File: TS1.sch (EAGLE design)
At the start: 20 parts, among them IC1 AT42QT1010, J1 PWR, Q1 2N7002

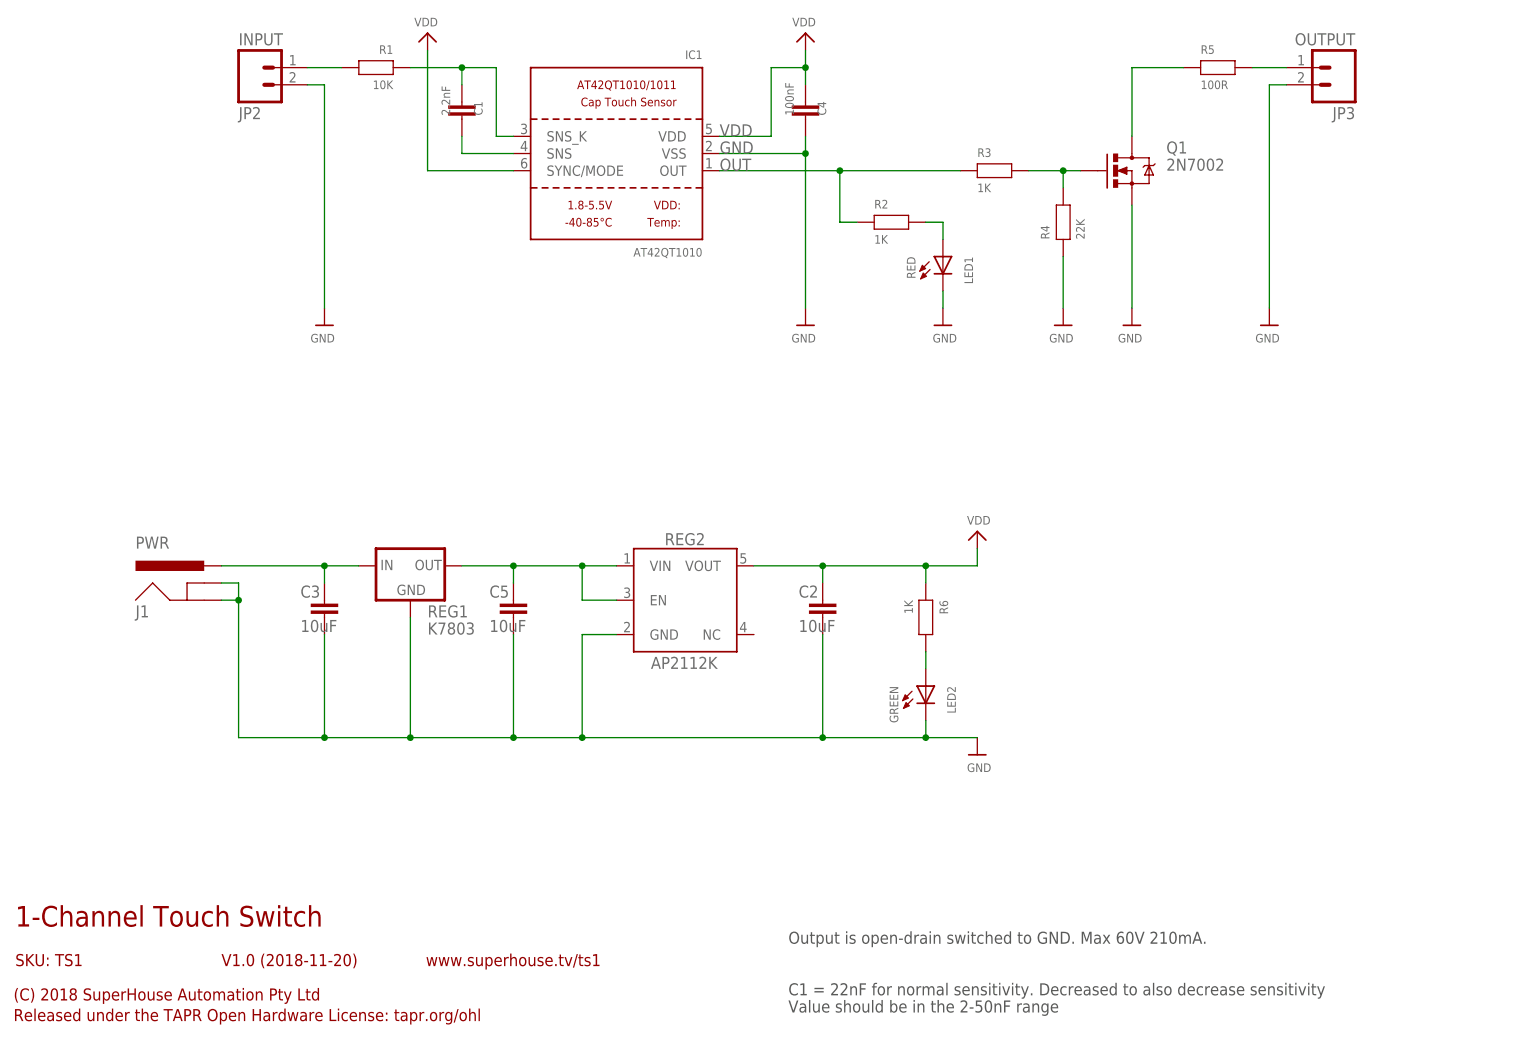
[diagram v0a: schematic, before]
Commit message: Pulled back GND plane around input to sensor IC to reduce capacitive loading
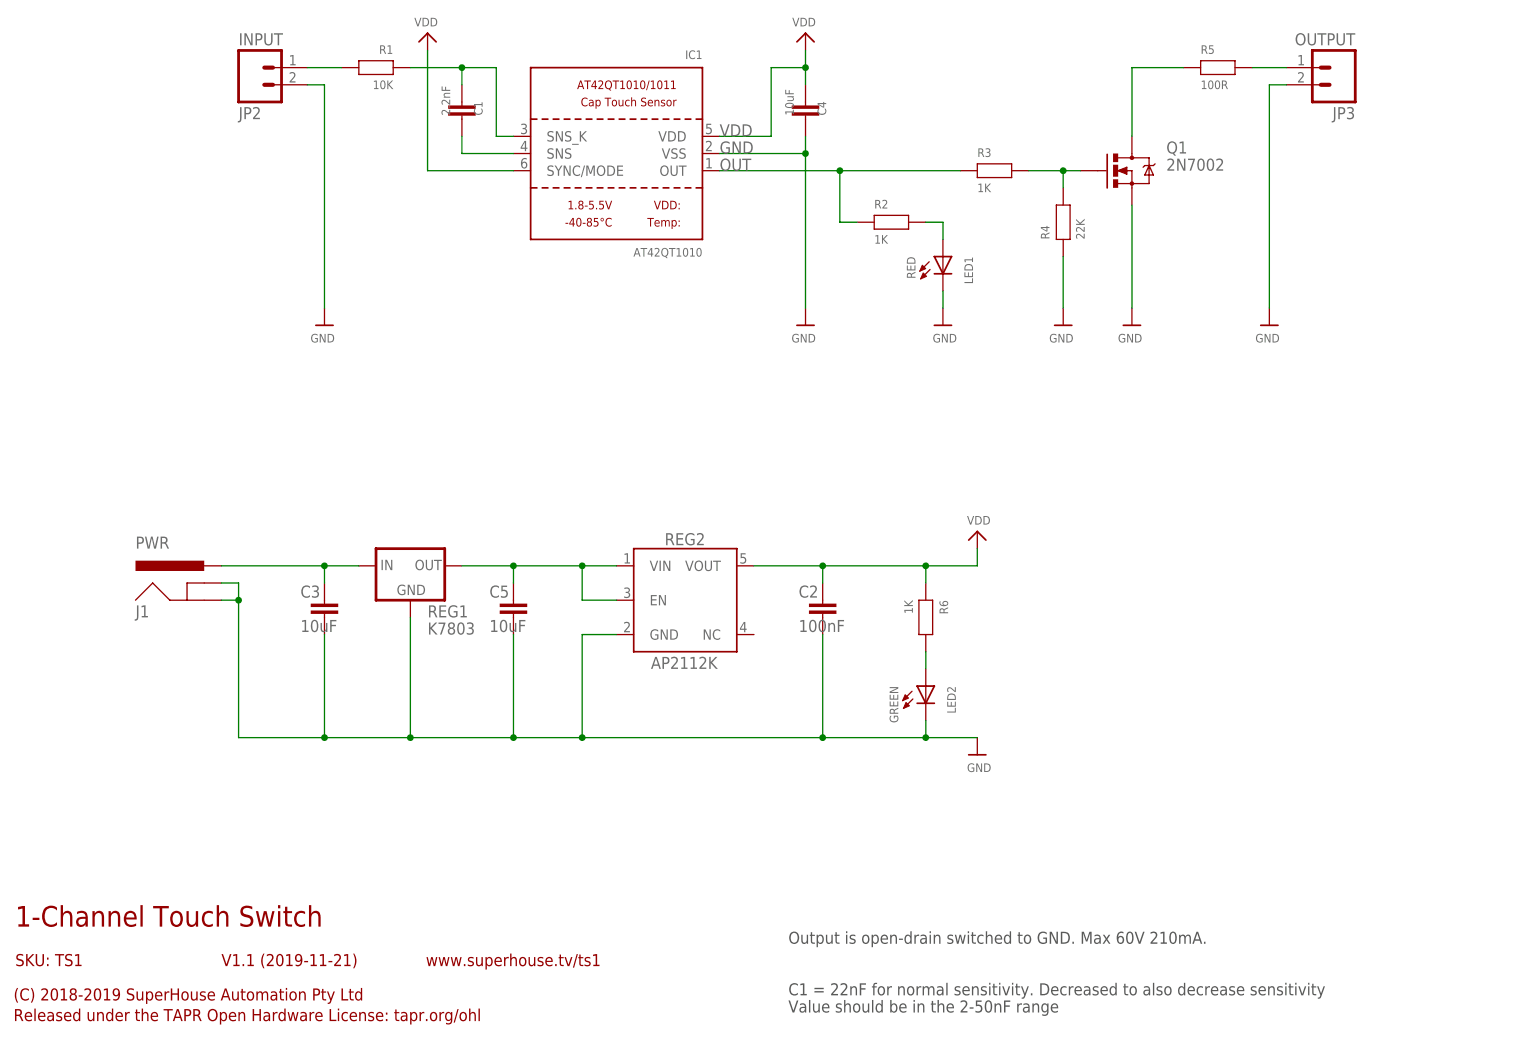
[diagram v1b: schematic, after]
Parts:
- C2: value 10uF -> 100nF
- C4: value 100nF -> 10uF
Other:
- note added: "(C) 2018-2019 SuperHouse Automation Pty Ltd"
- note added: "V1.1 (2019-11-21)"
- note removed: "(C) 2018 SuperHouse Automation Pty Ltd"
- note removed: "V1.0 (2018-11-20)"
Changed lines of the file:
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@@
 <?xml version="1.0" encoding="utf-8"?>
 <!DOCTYPE eagle SYSTEM "eagle.dtd">
-<eagle version="9.2.2">
+<eagle version="9.5.1">
 <drawing>
 <settings>
@@
 </classes>
 <parts>
-<part name="C2" library="freetronics-jon" library_urn="urn:adsk.eagle:library:7065448" deviceset="CAP" device="0603" package3d_urn="urn:adsk.eagle:package:7066315/2" value="10uF"/>
+<part name="C2" library="freetronics-jon" library_urn="urn:adsk.eagle:library:7065448" deviceset="CAP" device="0603" package3d_urn="urn:adsk.eagle:package:7066315/2" value="100nF"/>
 <part name="IC1" library="microbuilder" deviceset="AT42QT1010/1" device="" value="AT42QT1010"/>
 <part name="U$2" library="microbuilder" deviceset="GND" device=""/>
 <part name="C1" library="freetronics-jon" library_urn="urn:adsk.eagle:library:7065448" deviceset="CAP" device="0603" package3d_urn="urn:adsk.eagle:package:7066315/2" value="2.2nF"/>
 <part name="R1" library="freetronics-jon" library_urn="urn:adsk.eagle:library:7065448" deviceset="RESISTOR" device="0603" package3d_urn="urn:adsk.eagle:package:7066315/2" value="10K"/>
-<part name="C4" library="freetronics-jon" library_urn="urn:adsk.eagle:library:7065448" deviceset="CAP" device="0603" package3d_urn="urn:adsk.eagle:package:7066315/2" value="100nF"/>
+<part name="C4" library="freetronics-jon" library_urn="urn:adsk.eagle:library:7065448" deviceset="CAP" device="0603" package3d_urn="urn:adsk.eagle:package:7066315/2" value="10uF"/>
 <part name="U$3" library="microbuilder" deviceset="GND" device=""/>
 <part name="U$4" library="microbuilder" deviceset="VDD" device=""/>
@@
 <plain>
 <text x="7.62" y="20.32" size="3.048" layer="94">1-Channel Touch Switch</text>
-<text x="38.1" y="14.478" size="1.778" layer="94">V1.0 (2018-11-20)</text>
-<text x="7.366" y="9.398" size="1.778" layer="94">(C) 2018 SuperHouse Automation Pty Ltd</text>
+<text x="38.1" y="14.478" size="1.778" layer="94">V1.1 (2019-11-21)</text>
+<text x="7.366" y="9.398" size="1.778" layer="94">(C) 2018-2019 SuperHouse Automation Pty Ltd</text>
 <text x="7.366" y="6.35" size="1.778" layer="94">Released under the TAPR Open Hardware License: tapr.org/ohl</text>
 <text x="68.326" y="14.478" size="1.778" layer="94">www.superhouse.tv/ts1</text>

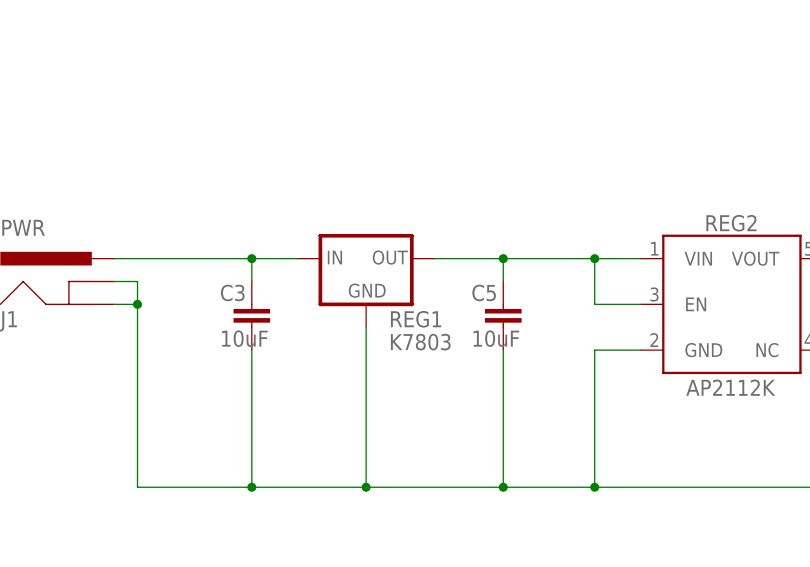
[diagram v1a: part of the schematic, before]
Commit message: Moved bypass cap closer to touch sensor IC
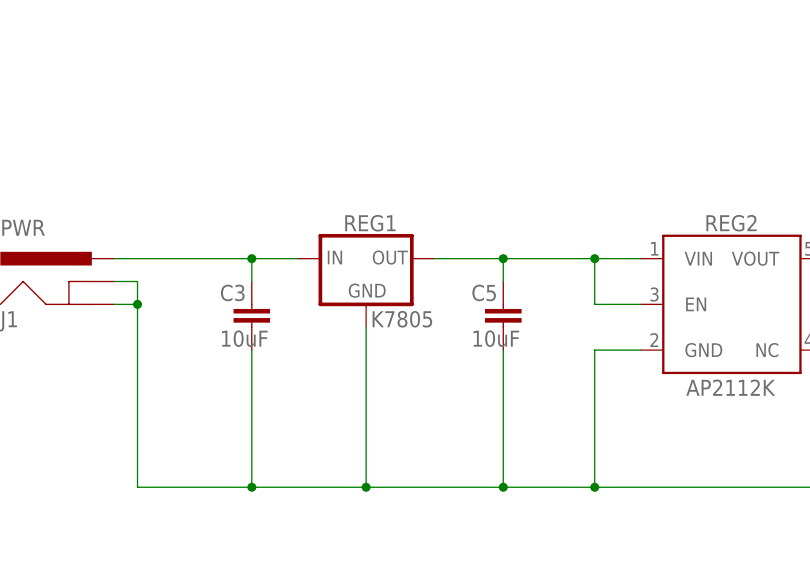
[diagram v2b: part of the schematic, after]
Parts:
- C1, C2, C3, C4, C5: device freetronics-jon:CAP0603 -> SuperHouse-DiscreteSemi:CAP0603
- IC1: device microbuilder:AT42QT1010/1 -> SuperHouse-ICs:AT42QT1010/1
- J1: device freetronics-jon:POWER_JACKPTH_SLOTS -> SuperHouse-Connectors:POWER_JACK-SLOTS
- JP2, JP3: device freetronics-jon:M02PTH -> SuperHouse-Connectors:M02-SOCKET
- LED1, LED2: device freetronics-jon:LED0603 -> SuperHouse-LEDs:LED0603
- Q1: device freetronics-jon:MOSFET-NSOT-323 -> SuperHouse-DiscreteSemi:MOSFET-NCHANNEL-233
- R1, R2, R3, R4, R5, R6: device freetronics-jon:RESISTOR0603 -> SuperHouse-DiscreteSemi:RESISTOR0603
- REG1: value K7803 -> K7805; device freetronics-jon:K78XX-500R3 -> SuperHouse-Regulators:K78XX-500R3
- REG2: device freetronics-jon:AP2112KSOT25 -> SuperHouse-Regulators:AP2112KSOT25
